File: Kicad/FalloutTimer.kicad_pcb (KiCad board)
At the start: 2 copper layers, 6 parts, among them J1 Conn_01x05_Pin, SW1 SW_Push, SW2 SW_Push, U1 DS3231M

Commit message: added an outline for the display on the pcb
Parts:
- removed J1: Conn_01x05_Pin, Connector_PinHeader_2.54mm:PinHeader_1x05_P2.54mm_Vertical
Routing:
- net /DIO: track 48.3 -> 6.64 mm
- net /SCK: track 51.7 -> 10.4 mm
- net GND: track 55.1 -> 41.6 mm
- net +5V: track 67.9 -> 54.7 mm
- net /RCK: track 49.9 -> 41.3 mm

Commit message: Finsihed PCB.
asdasd
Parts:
- added G***: LOGO, LOGO, B.Cu at (120.0, 77.5)
- added J1: Conn_01x05_Pin, Connector_PinHeader_2.54mm:PinHeader_1x05_P2.54mm_Vertical, F.Cu at (100.5, 73.9)
- added REF**: 7seg, 7SegDisplay:7seg, F.Cu at (108.5, 78.0)
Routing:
- net GND: track 41.6 -> 176.7 mm
- net /DIO: track 6.64 -> 47.9 mm
- net /SCK: track 10.4 -> 51.2 mm
- net +5V: track 54.7 -> 67.5 mm
- net /RCK: track 41.3 -> 51.8 mm
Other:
- board outline added: 53 x 56.5 mm
- board text added: "Made By Joseph Stein For Hack Club Fallout"

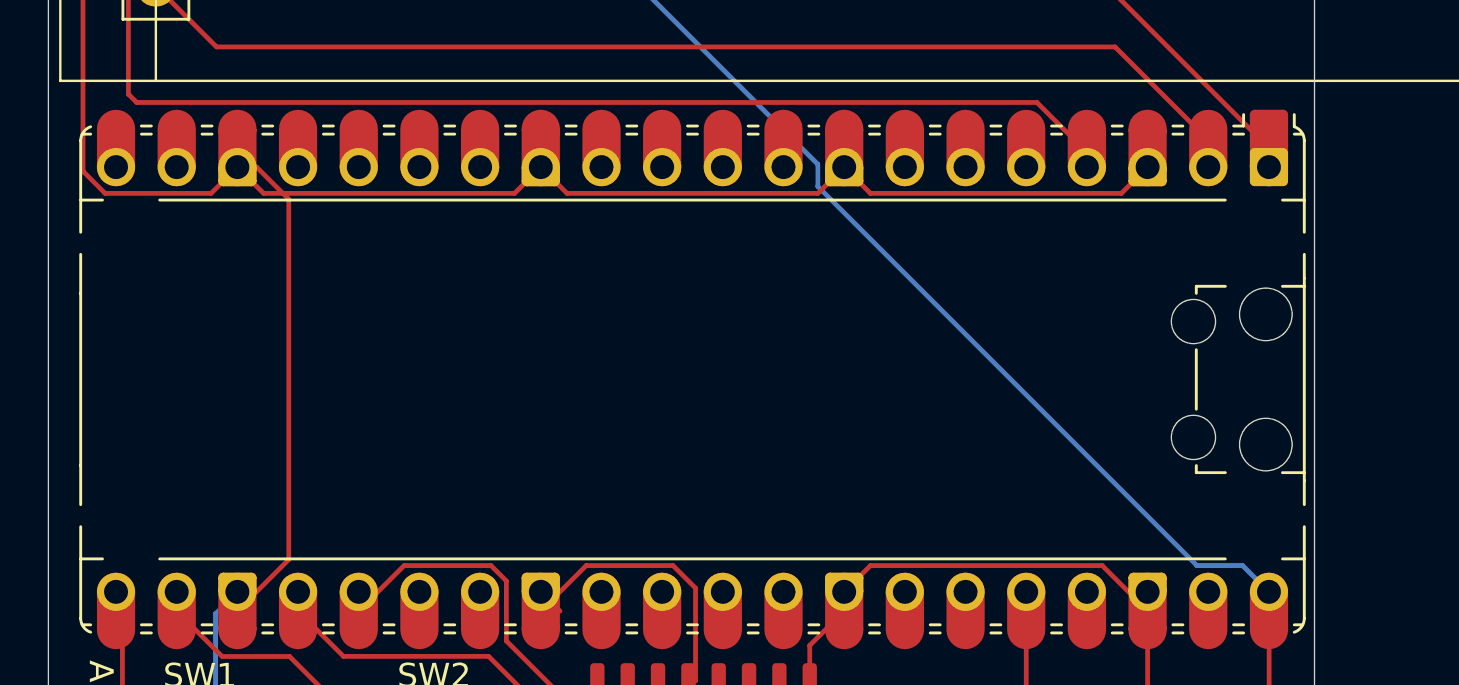
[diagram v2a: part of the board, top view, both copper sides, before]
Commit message: Janky hopefully precise enough screw holes
i basically just put them where the pico holes are.
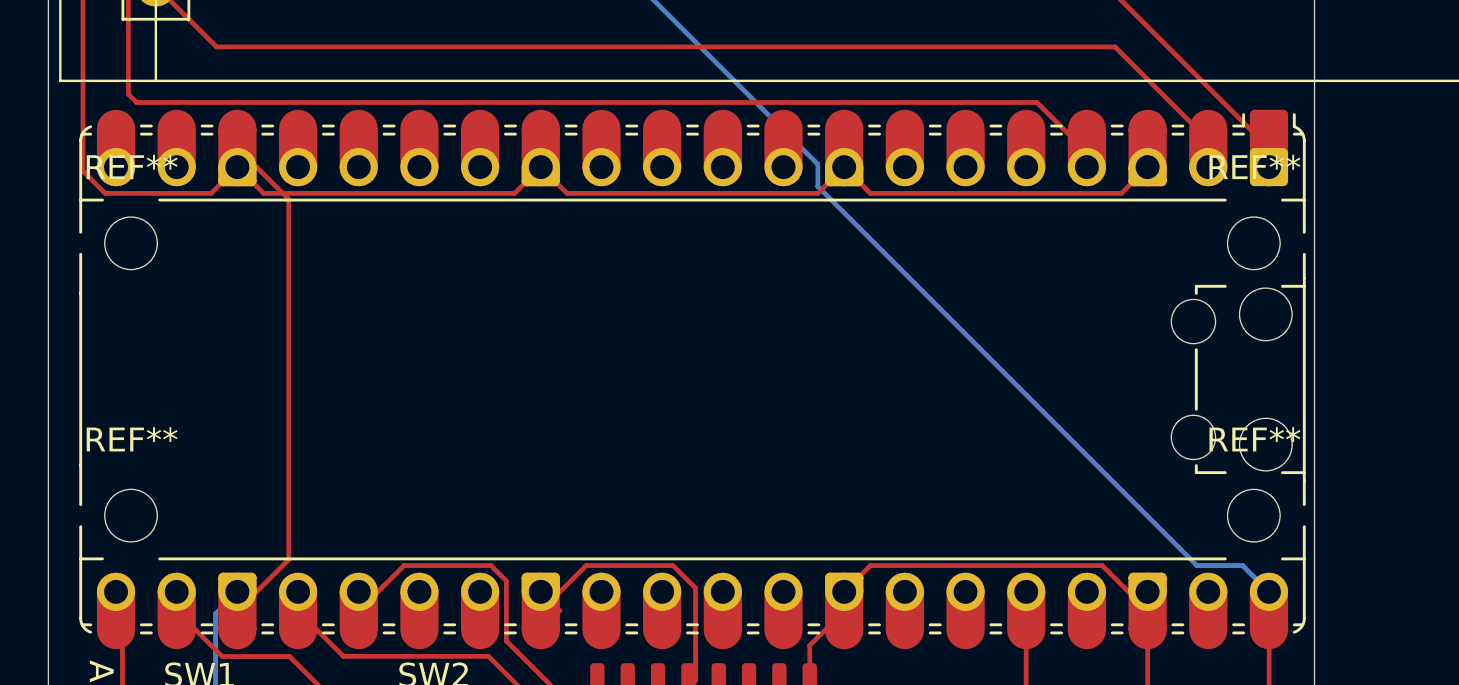
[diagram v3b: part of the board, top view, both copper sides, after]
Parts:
- added REF**: MountingHole_2.2mm_M2, MountingHole:MountingHole_2.2mm_M2, F.Cu at (146.5, 94.8)
- added REF**: MountingHole_2.2mm_M2, MountingHole:MountingHole_2.2mm_M2, F.Cu at (146.5, 106.2)
- added REF**: MountingHole_2.2mm_M2, MountingHole:MountingHole_2.2mm_M2, F.Cu at (99.5, 106.2)
- added REF**: MountingHole_2.2mm_M2, MountingHole:MountingHole_2.2mm_M2, F.Cu at (99.5, 94.8)
